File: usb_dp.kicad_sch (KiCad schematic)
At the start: 60 parts, among them J9 USB-C_WE_632723300011, U30 TPS65988DHRSHR, U33 TUSB1046-DCIRNQ, U35 AP22615A_TSOT26, U36 TPD4E05U06QDQARQ1, U37 TPD4E05U06QDQARQ1, U38 TPD4E05U06QDQARQ1, U41 TPD4E05U06QDQARQ1

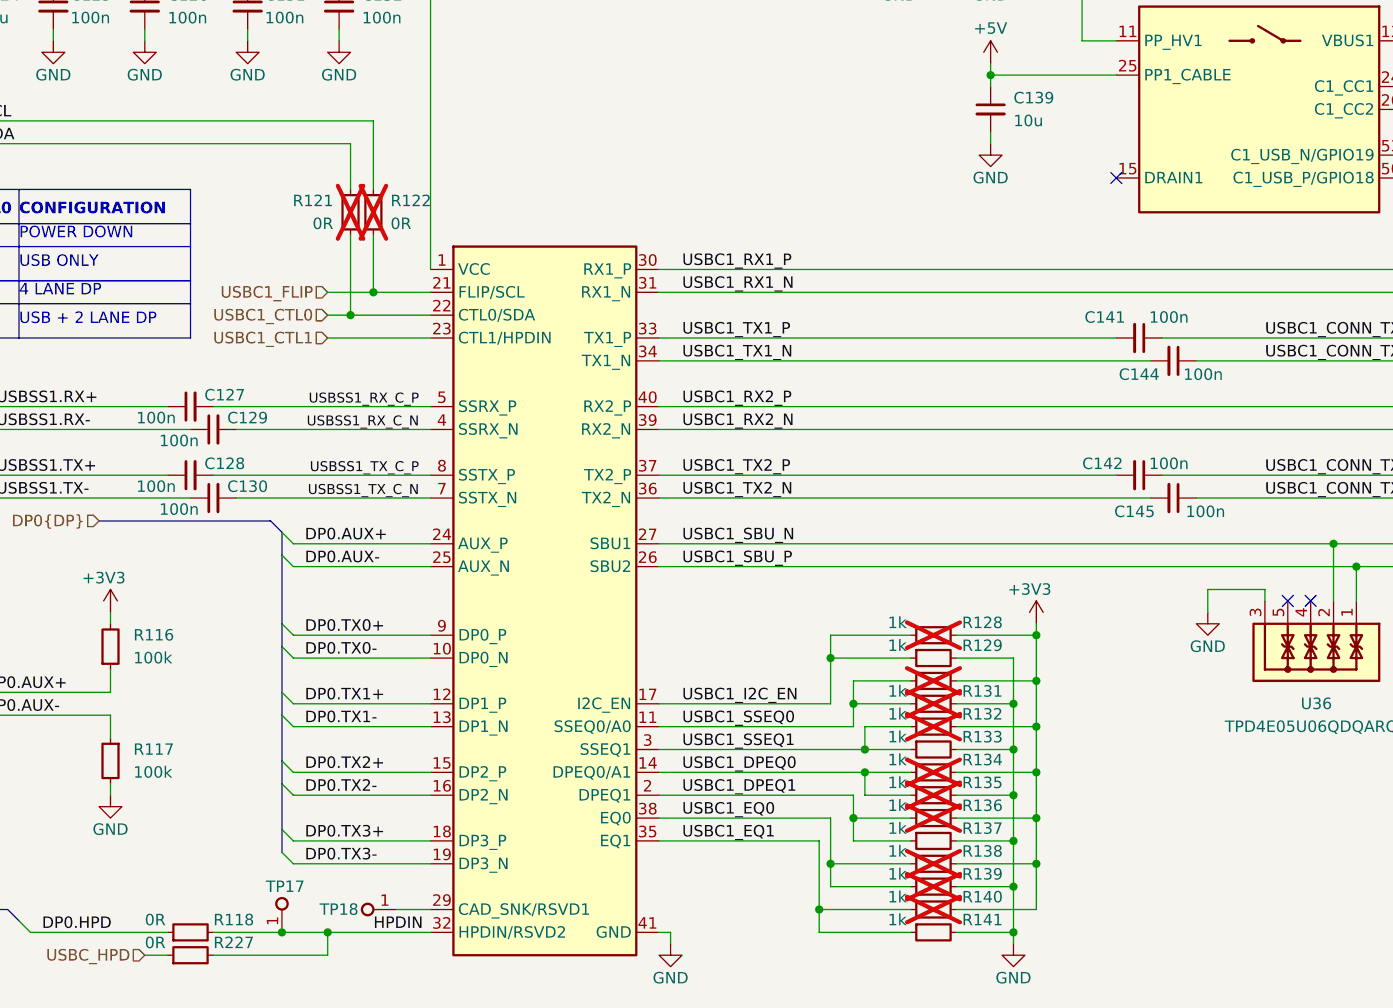
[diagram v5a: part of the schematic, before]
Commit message: [#83224] Place USB DP Alt mode
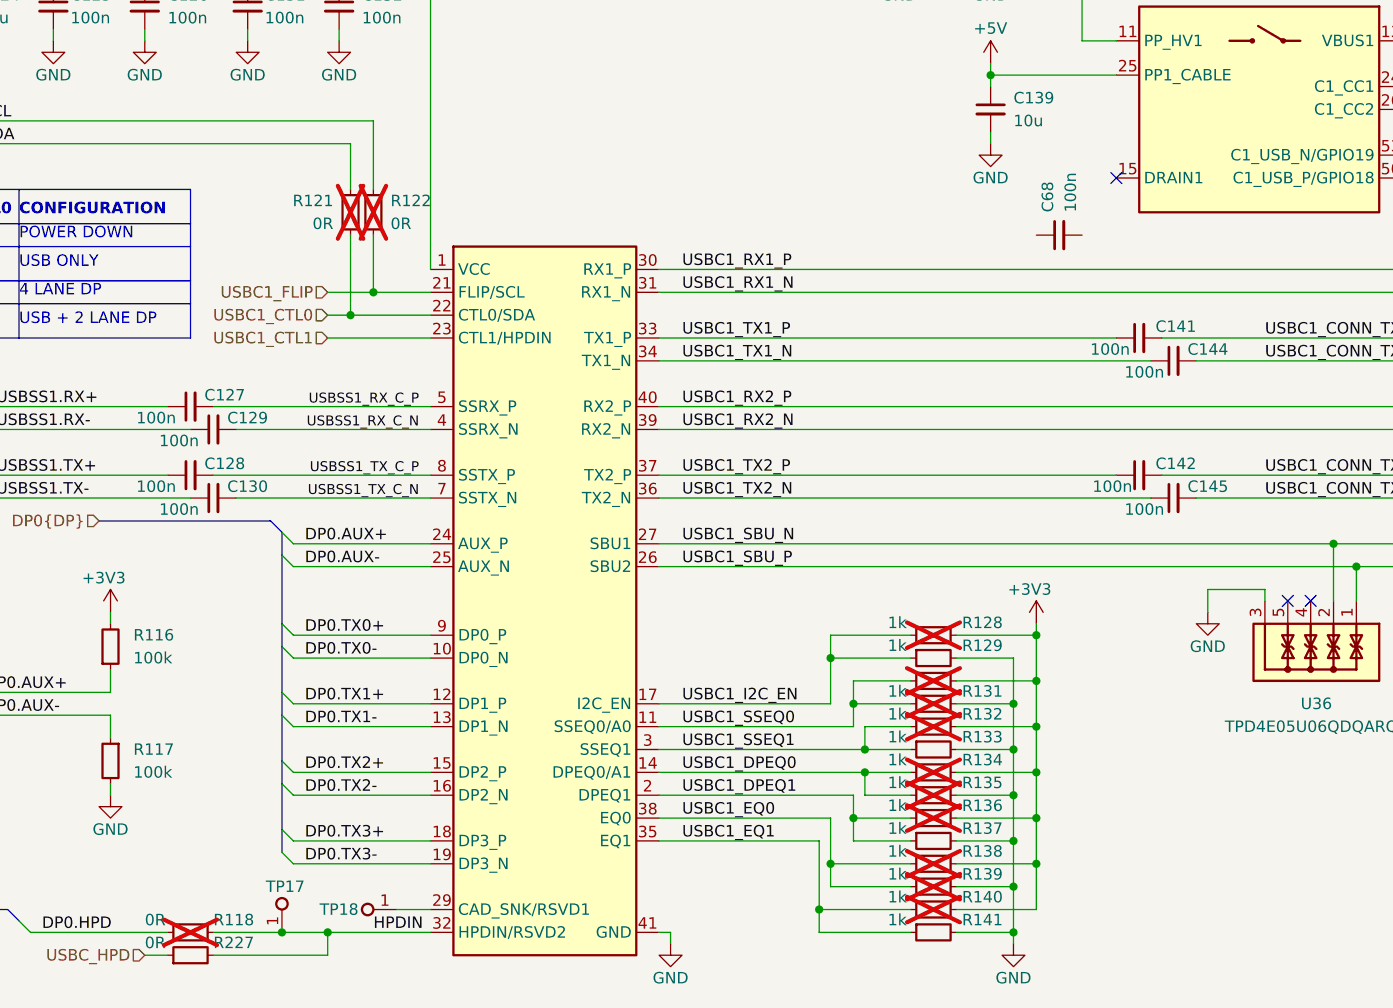
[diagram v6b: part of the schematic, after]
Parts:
- removed C141, C142, C144, C145: C_100n_0201, antmicro-footprints:C_0201, symbol antmicroCapacitorsmisc:C_100n_0201
- added C141, C142, C144, C145, C68: C_100n_0402, antmicro-footprints:C_0402_1005Metric, symbol antmicroCapacitors0402:C_100n_0402
- R118: now not fitted
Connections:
- net USBC1_CONN_TX1_N: now also C144.2
- net USBC1_CONN_TX1_P: now also C141.2
- net USBC1_CONN_TX2_N: now also C145.2
- net USBC1_CONN_TX2_P: now also C142.2
- net USBC1_TX1_N: now also C144.1
- net USBC1_TX1_P: now also C141.1
- net USBC1_TX2_N: now also C145.1
- net USBC1_TX2_P: now also C142.1

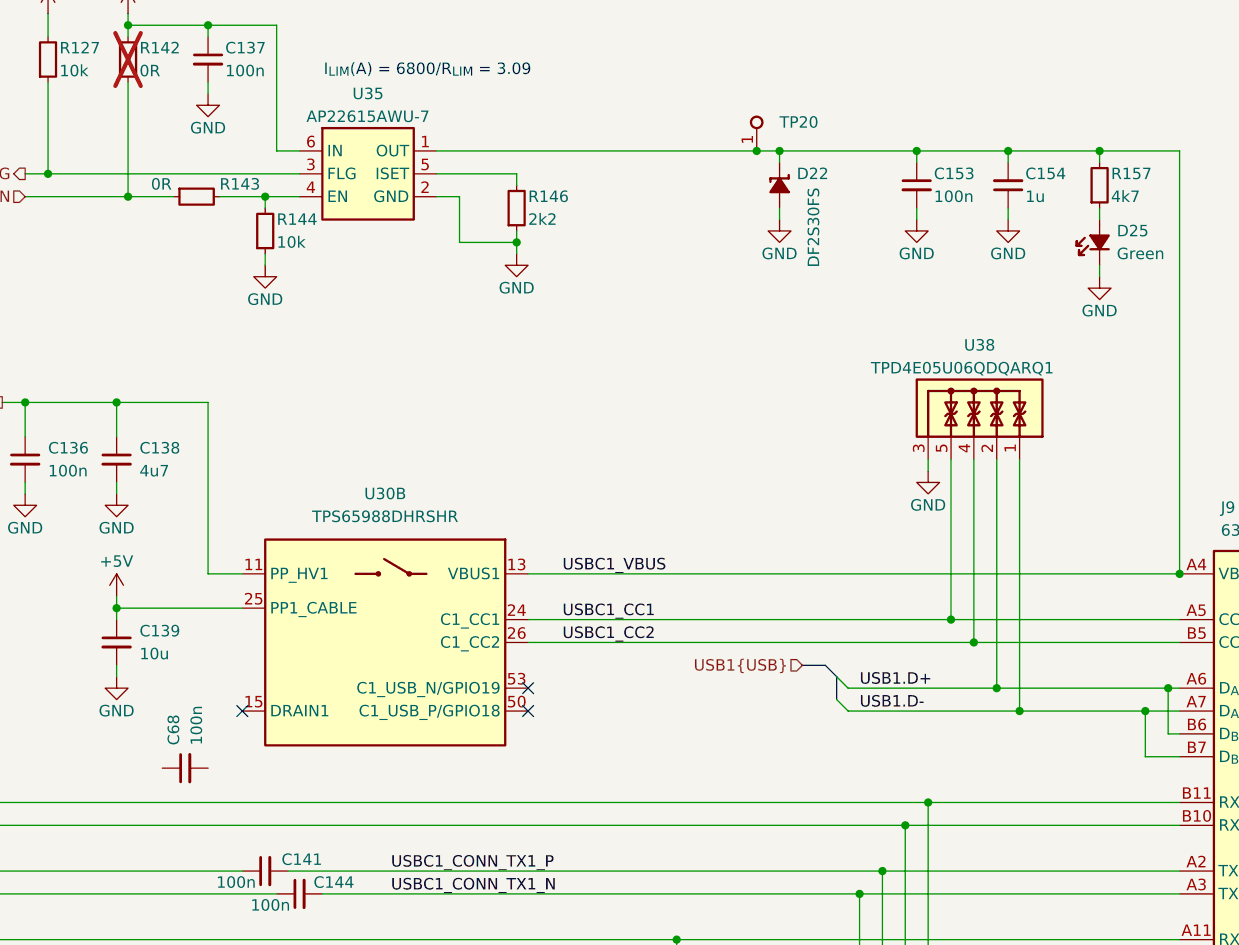
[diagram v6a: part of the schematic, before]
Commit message: [#83224] Add AC coupling capacitors to USBSS
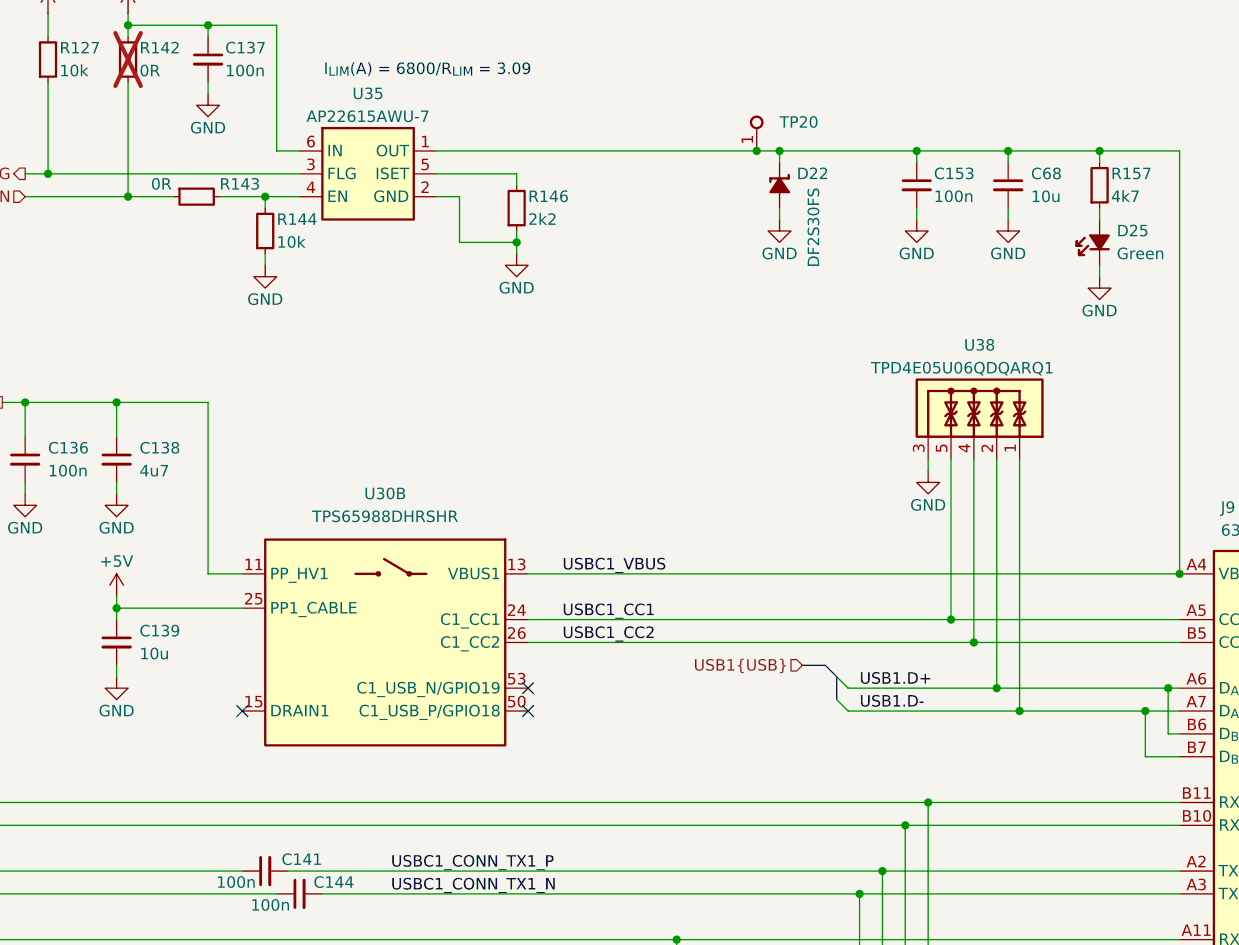
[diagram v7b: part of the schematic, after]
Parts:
- removed C154: C_1u_25V_0402, antmicro-footprints:C_0402_1005Metric, symbol antmicroCapacitors0402:C_1u_25V_0402
- removed C68: C_100n_0402, antmicro-footprints:C_0402_1005Metric, symbol antmicroCapacitors0402:C_100n_0402
- added C68: C_10u_0603, antmicro-footprints:C_0603_1608Metric, symbol antmicroCapacitors0603:C_10u_0603
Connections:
- net GND: now also C68.2
- net USBC1_VBUS: now also C68.1
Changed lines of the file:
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@@
 	)
 	(symbol
-		(lib_id "antmicroCapacitors0402:C_1u_25V_0402")
-		(at 287.02 69.85 90)
-		(unit 1)
-		(exclude_from_sim no)
-		(in_bom yes)
-		(on_board yes)
-		(dnp no)
-		(property "Reference" "C154"
-			(at 288.925 66.04 90)
-			(effects
-				(font
-					(size 1.27 1.27)
-				)
-				(justify right)
-			)
-		)
-		(property "Value" "C_1u_25V_0402"
-			(at 297.18 49.53 0)
-			(effects
-				(font
-					(size 1.27 1.27)
-					(thickness 0.15)
-				)
-				(justify left bottom)
-				(hide yes)
-			)
-		)
-		(property "Footprint" "antmicro-footprints:C_0402_1005Metric"
-			(at 299.72 49.53 0)
-			(effects
-				(font
-					(size 1.27 1.27)
-					(thickness 0.15)
-				)
-				(justify left bottom)
-				(hide yes)
-			)
-		)
-		(property "Datasheet" "https://www.murata.com/products/productdetail?partno=GRM155R61E105KE11%23"
-			(at 302.26 49.53 0)
-			(effects
-				(font
-					(size 1.27 1.27)
-					(thickness 0.15)
-				)
-				(justify left bottom)
-				(hide yes)
-			)
-		)
-		(property "Description" ""
-			(at 287.02 69.85 0)
-			(effects
-				(font
-					(size 1.27 1.27)
-				)
-				(hide yes)
-			)
-		)
-		(property "Manufacturer" "Murata"
-			(at 307.34 49.53 0)
-			(effects
-				(font
-					(size 1.27 1.27)
-					(thickness 0.15)
-				)
-				(justify left bottom)
-				(hide yes)
-			)
-		)
-		(property "MPN" "GRM155R61E105KE11J"
-			(at 304.8 49.53 0)
-			(effects
-				(font
-					(size 1.27 1.27)
-					(thickness 0.15)
-				)
-				(justify left bottom)
-				(hide yes)
-			)
-		)
-		(property "Val" "1u"
-			(at 288.925 68.58 90)
-			(effects
-				(font
-					(size 1.27 1.27)
-					(thickness 0.15)
-				)
-				(justify right)
-			)
-		)
-		(property "License" "Apache-2.0"
-			(at 309.88 49.53 0)
-			(effects
-				(font
-					(size 1.27 1.27)
-					(thickness 0.15)
-				)
-				(justify left bottom)
-				(hide yes)
-			)
-		)
-		(property "Author" "Antmicro"
-			(at 312.42 49.53 0)
-			(effects
-				(font
-					(size 1.27 1.27)
-					(thickness 0.15)
-				)
-				(justify left bottom)
-				(hide yes)
-			)
-		)
-		(property "Voltage" "25V"
-			(at 314.96 49.53 0)
-			(effects
-				(font
-					(size 1.27 1.27)
-				)
-				(justify left bottom)
-				(hide yes)
-			)
-		)
-		(property "Dielectric" "X5R"
-			(at 317.5 49.53 0)
-			(effects
-				(font
-					(size 1.27 1.27)
-				)
-				(justify left bottom)
-				(hide yes)
-			)
-		)
-		(pin "1"
-		)
-		(pin "2"
-		)
-		(instances
-			(project "jetson-agx-thor-baseboard"
-				(path "/f569b0be-0afd-48b7-93ee-28582a4c645c/79924a89-4330-4c0a-9aa5-2a2f90ef321b"
-					(reference "C154")
-					(unit 1)
-				)
-			)
-		)
-	)
-	(symbol
 		(lib_id "antmicroResistors0402:R_100k_0402")
 		(at 90.17 187.96 270)
@@
 	)
 	(symbol
-		(lib_id "antmicroCapacitors0402:C_100n_0402")
-		(at 193.04 132.08 0)
-		(mirror x)
-		(unit 1)
-		(exclude_from_sim no)
-		(in_bom yes)
-		(on_board yes)
-		(dnp no)
-		(property "Reference" "C68"
-			(at 194.3163 129.54 90)
-			(effects
-				(font
-					(size 1.27 1.27)
-				)
-				(justify right)
-			)
-		)
-		(property "Value" "C_100n_0402"
-			(at 213.36 121.92 0)
-			(effects
-				(font
-					(size 1.27 1.27)
-					(thickness 0.15)
-				)
-				(justify left bottom)
-				(hide yes)
-			)
-		)
-		(property "Footprint" "antmicro-footprints:C_0402_1005Metric"
-			(at 213.36 119.38 0)
-			(effects
-				(font
-					(size 1.27 1.27)
-					(thickness 0.15)
-				)
-				(justify left bottom)
-				(hide yes)
-			)
-		)
-		(property "Datasheet" "https://www.murata.com/products/productdetail?partno=GRM155R61H104KE14%23"
-			(at 213.36 116.84 0)
-			(effects
-				(font
-					(size 1.27 1.27)
-					(thickness 0.15)
-				)
-				(justify left bottom)
-				(hide yes)
-			)
-		)
-		(property "Description" ""
-			(at 193.04 132.08 0)
-			(effects
-				(font
-					(size 1.27 1.27)
-				)
-				(hide yes)
-			)
-		)
-		(property "Manufacturer" "Murata"
-			(at 213.36 111.76 0)
-			(effects
-				(font
-					(size 1.27 1.27)
-					(thickness 0.15)
-				)
-				(justify left bottom)
-				(hide yes)
-			)
-		)
-		(property "MPN" "GRM155R61H104KE14D"
-			(at 213.36 114.3 0)
-			(effects
-				(font
-					(size 1.27 1.27)
-					(thickness 0.15)
-				)
-				(justify left bottom)
-				(hide yes)
-			)
-		)
-		(property "Val" "100n"
-			(at 196.8563 129.54 90)
-			(effects
-				(font
-					(size 1.27 1.27)
-					(thickness 0.15)
-				)
-				(justify right)
-			)
-		)
-		(property "License" "Apache-2.0"
-			(at 213.36 109.22 0)
-			(effects
-				(font
-					(size 1.27 1.27)
-					(thickness 0.15)
-				)
-				(justify left bottom)
-				(hide yes)
-			)
-		)
-		(property "Author" "Antmicro"
-			(at 213.36 106.68 0)
-			(effects
-				(font
-					(size 1.27 1.27)
-					(thickness 0.15)
-				)
-				(justify left bottom)
-				(hide yes)
-			)
-		)
-		(property "Voltage" "50V"
-			(at 213.36 104.14 0)
-			(effects
-				(font
-					(size 1.27 1.27)
-				)
-				(justify left bottom)
-				(hide yes)
-			)
-		)
-		(property "Dielectric" "X5R"
-			(at 213.36 101.6 0)
-			(effects
-				(font
-					(size 1.27 1.27)
-				)
-				(justify left bottom)
-				(hide yes)
-			)
-		)
-		(pin "1"
-		)
-		(pin "2"
-		)
-		(instances
-			(project "jetson-agx-thor-baseboard"
-				(path "/f569b0be-0afd-48b7-93ee-28582a4c645c/79924a89-4330-4c0a-9aa5-2a2f90ef321b"
-					(reference "C68")
-					(unit 1)
-				)
-			)
-		)
-	)
-	(symbol
 		(lib_id "antmicroInterfaceControllers:TUSB1046-DCIRNQ")
 		(at 125.73 135.89 0)
@@
 					(unit 1)
 				)
+			)
+		)
+	)
+	(symbol
+		(lib_id "antmicroCapacitors0603:C_10u_0603")
+		(at 287.02 64.77 90)
+		(mirror x)
+		(unit 1)
+		(exclude_from_sim no)
+		(in_bom yes)
+		(on_board yes)
+		(dnp no)
+		(fields_autoplaced yes)
+		(property "Reference" "C68"
+			(at 289.56 66.0463 90)
+			(effects
+				(font
+					(size 1.27 1.27)
+				)
+				(justify right)
+			)
+		)
+		(property "Value" "C_10u_0603"
+			(at 297.18 85.09 0)
+			(effects
+				(font
+					(size 1.27 1.27)
+					(thickness 0.15)
+				)
+				(justify left bottom)
+				(hide yes)
+			)
+		)
+		(property "Footprint" "antmicro-footprints:C_0603_1608Metric"
+			(at 299.72 85.09 0)
+			(effects
+				(font
+					(size 1.27 1.27)
+					(thickness 0.15)
+				)
+				(justify left bottom)
+				(hide yes)
+			)
+		)
+		(property "Datasheet" "https://www.murata.com/products/productdetail?partno=GRM188R61A106KE69%23"
+			(at 302.26 85.09 0)
+			(effects
+				(font
+					(size 1.27 1.27)
+					(thickness 0.15)
+				)
+				(justify left bottom)
+				(hide yes)
+			)
+		)
+		(property "Description" ""
+			(at 287.02 64.77 0)
+			(effects
+				(font
+					(size 1.27 1.27)
+				)
+				(hide yes)
+			)
+		)
+		(property "Manufacturer" "Murata"
+			(at 307.34 85.09 0)
+			(effects
+				(font
+					(size 1.27 1.27)
+					(thickness 0.15)
+				)
+				(justify left bottom)
+				(hide yes)
+			)
+		)
+		(property "MPN" "GRM188R61A106KE69D"
+			(at 304.8 85.09 0)
+			(effects
+				(font
+					(size 1.27 1.27)
+					(thickness 0.15)
+				)
+				(justify left bottom)
+				(hide yes)
+			)
+		)
+		(property "Val" "10u"
+			(at 289.56 68.5863 90)
+			(effects
+				(font
+					(size 1.27 1.27)
+					(thickness 0.15)
+				)
+				(justify right)
+			)
+		)
+		(property "License" "Apache-2.0"
+			(at 309.88 85.09 0)
+			(effects
+				(font
+					(size 1.27 1.27)
+					(thickness 0.15)
+				)
+				(justify left bottom)
+				(hide yes)
+			)
+		)
+		(property "Author" "Antmicro"
+			(at 312.42 85.09 0)
+			(effects
+				(font
+					(size 1.27 1.27)
+					(thickness 0.15)
+				)
+				(justify left bottom)
+				(hide yes)
+			)
+		)
+		(property "Voltage" ""
+			(at 314.96 85.09 0)
+			(effects
+				(font
+					(size 1.27 1.27)
+				)
+				(justify left bottom)
+				(hide yes)
+			)
+		)
+		(property "Dielectric" "template_dielectric"
+			(at 317.5 85.09 0)
+			(effects
+				(font
+					(size 1.27 1.27)
+				)
+				(justify left bottom)
+				(hide yes)
+			)
+		)
+		(pin "1"
+		)
+		(pin "2"
+		)
+		(instances
+			(project "jetson-agx-thor-baseboard"
+				(path "/f569b0be-0afd-48b7-93ee-28582a4c645c/79924a89-4330-4c0a-9aa5-2a2f90ef321b"
+					(reference "C68")
+					(unit 1)
+				)

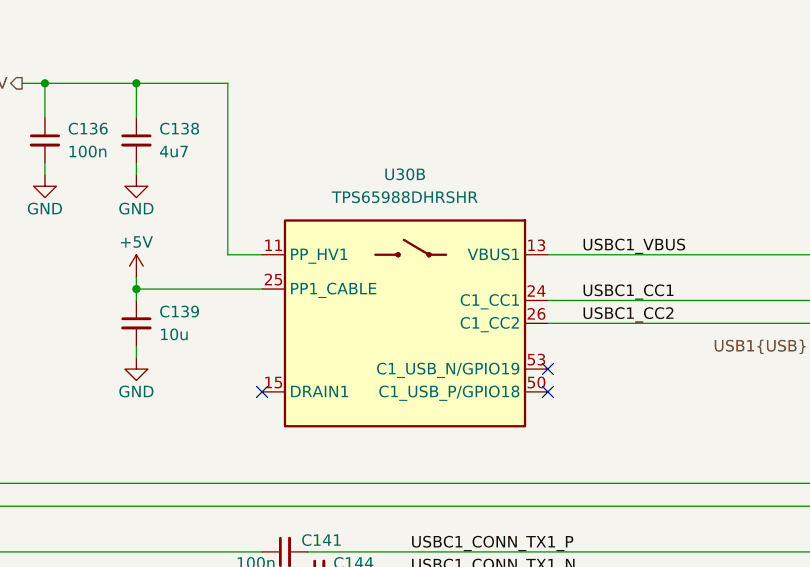
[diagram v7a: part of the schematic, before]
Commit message: [#83224] Place USB Debug section
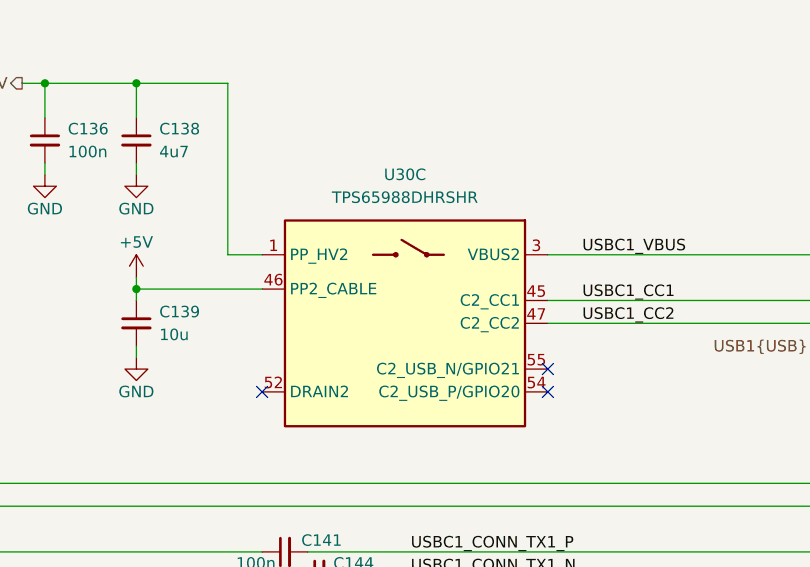
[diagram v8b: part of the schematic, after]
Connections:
- net +5V: now also U30.46 (PP2_CABLE); no longer U30.25 (PP1_CABLE)
- net USBC1_CC1: now also U30.45 (C2_CC1); no longer U30.24 (C1_CC1)
- net USBC1_CC2: now also U30.47 (C2_CC2); no longer U30.26 (C1_CC2)
- net USBC1_VBUS: now also U30.3 (VBUS2); no longer U30.13 (VBUS1)
- net USBPD1_HV: now also U30.1 (PP_HV2); no longer U30.11 (PP_HV1)
- new net: U30.52 (DRAIN2), U30.56 (DRAIN2), U30.57 (DRAIN2), U30.7 (DRAIN2)
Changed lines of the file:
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@@
 		(at 233.68 110.49 0)
 		(mirror y)
-		(unit 2)
+		(unit 3)
 		(exclude_from_sim no)
 		(in_bom yes)
@@
 				(path "/f569b0be-0afd-48b7-93ee-28582a4c645c/79924a89-4330-4c0a-9aa5-2a2f90ef321b"
 					(reference "U30")
-					(unit 2)
-				)
-			)
+					(unit 3)
+				)
+			)
